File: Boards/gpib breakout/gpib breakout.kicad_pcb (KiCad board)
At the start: 2 copper layers, 51.7 x 66 mm, 18 parts, among them J1 2x12 card edge connector (let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, J2 112-024-113R001, J3 Raspberry_Pi_2_3, U1 SN75160BN, U2 SN75161BN

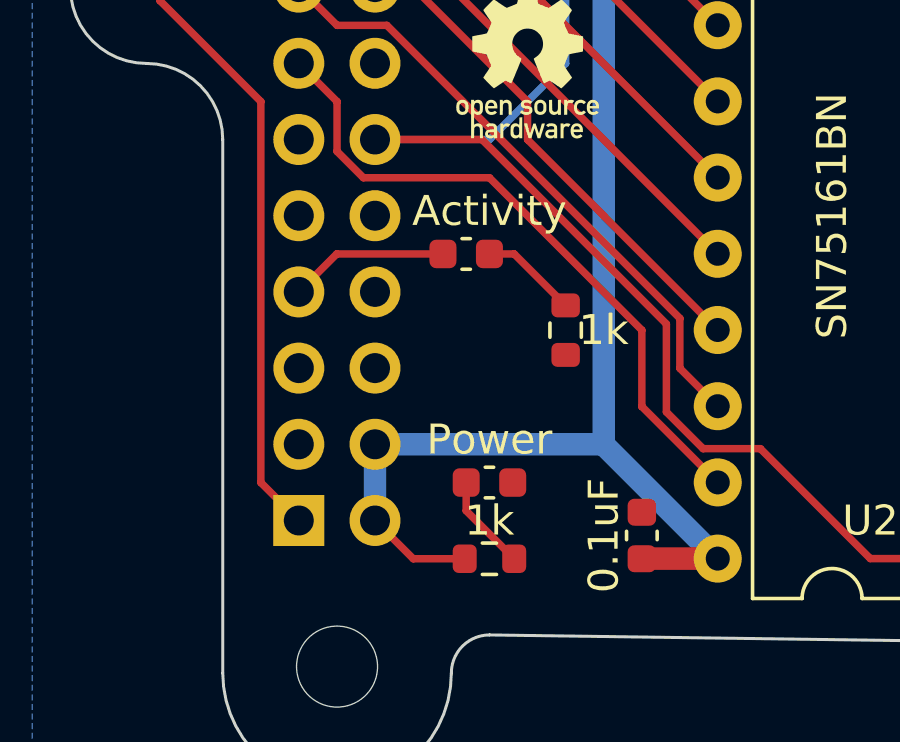
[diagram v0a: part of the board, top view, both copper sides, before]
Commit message: moved LEDs to the other side of the board
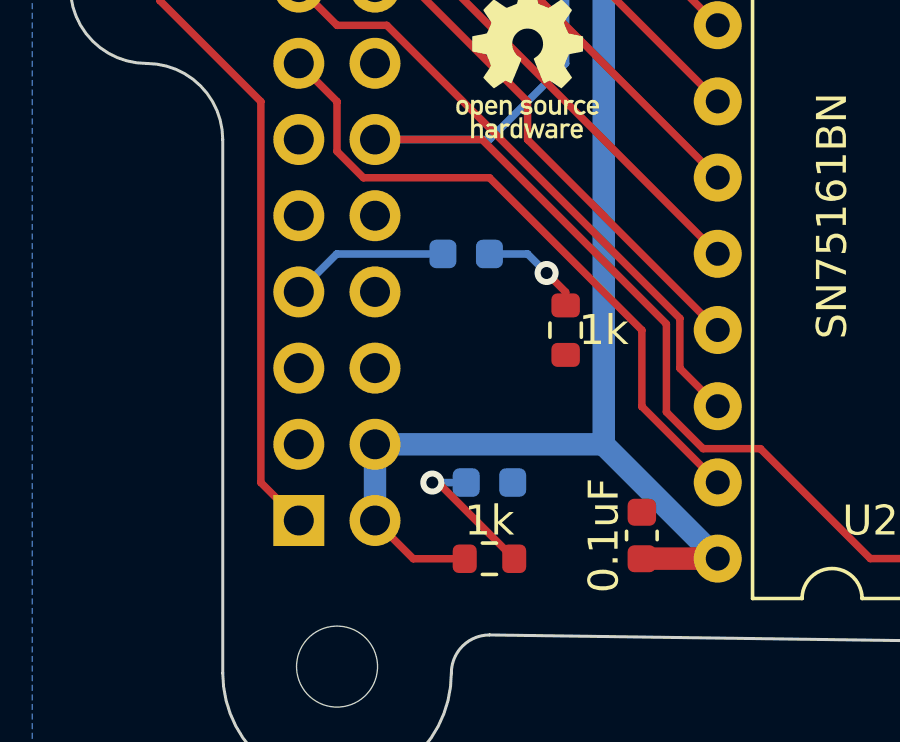
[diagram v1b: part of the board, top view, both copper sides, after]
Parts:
- D1, D2: moved to B.Cu
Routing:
- net Net-(D2-Pad2): track 3.20 -> 4.91 mm, vias 0 -> 1
- net Net-(D1-Pad1): track 3.25 -> 3.51 mm, vias 0 -> 1

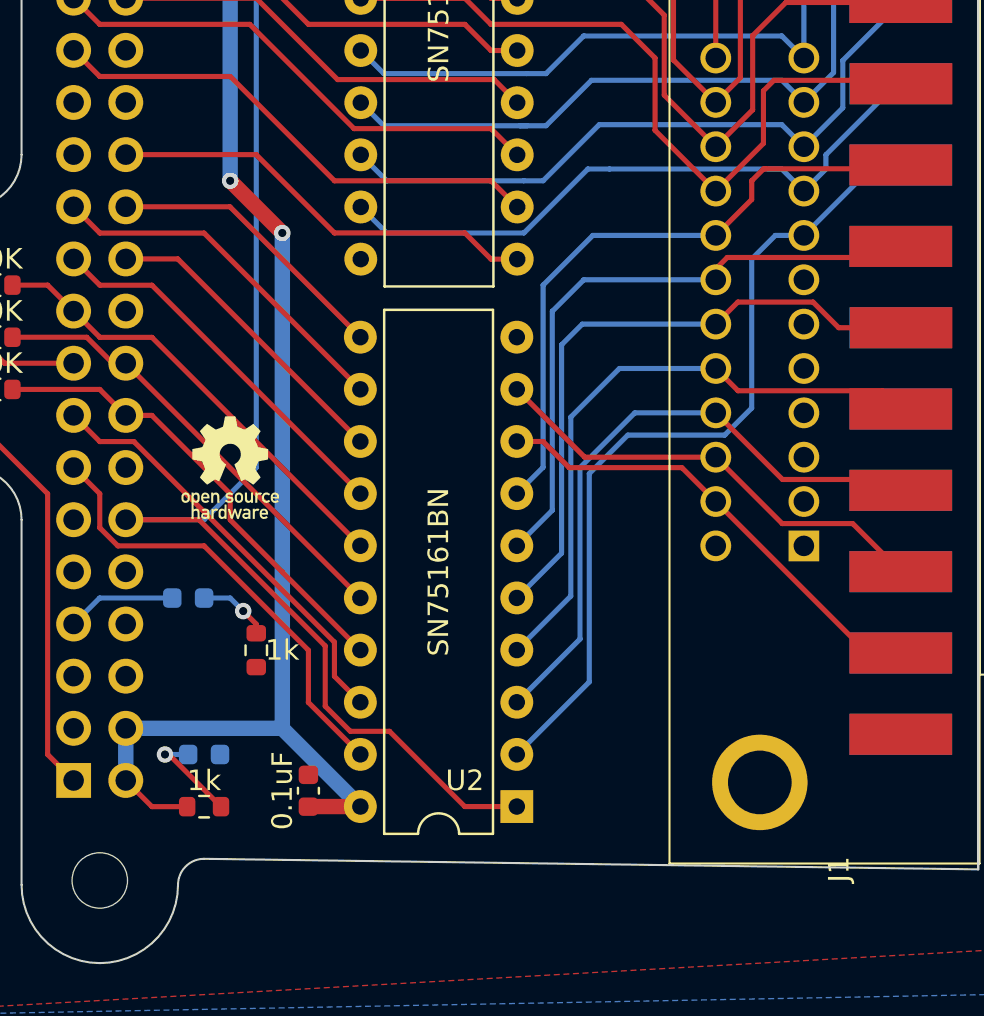
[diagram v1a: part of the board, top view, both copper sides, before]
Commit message: added gitignore
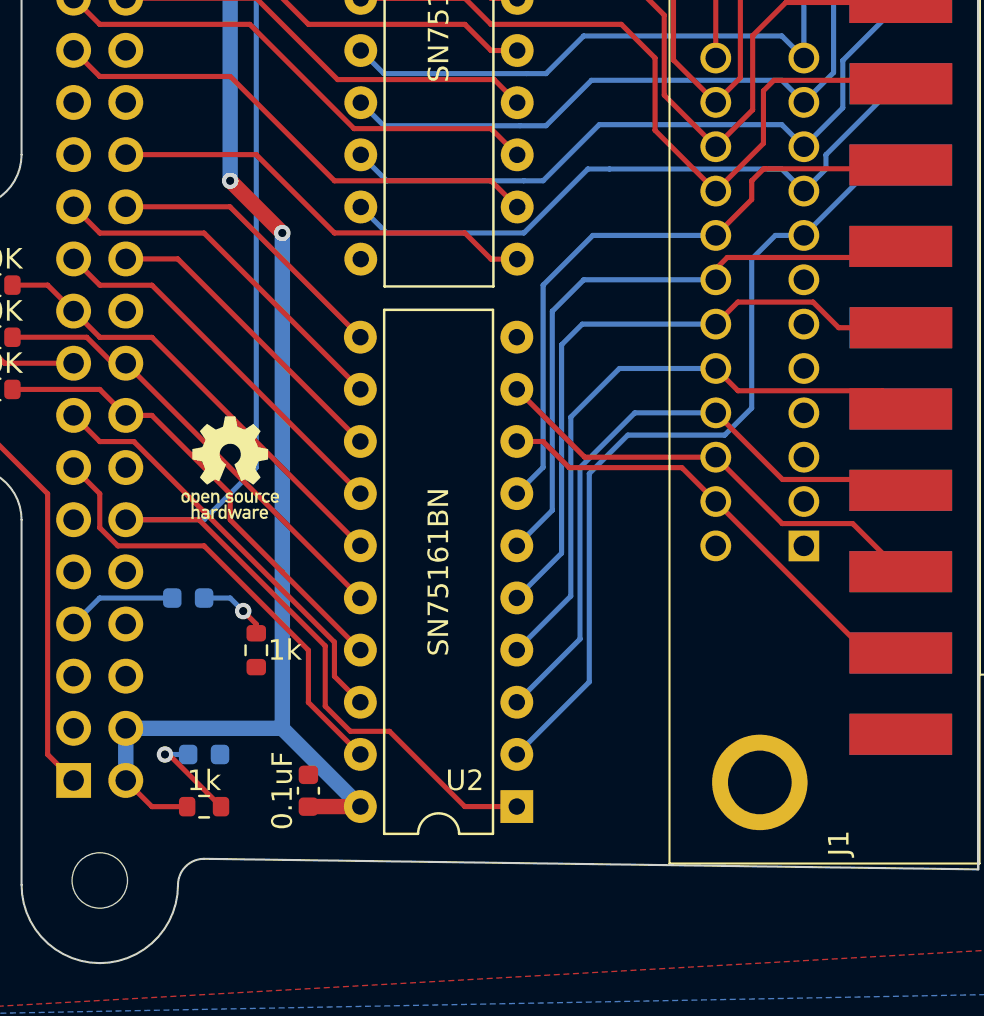
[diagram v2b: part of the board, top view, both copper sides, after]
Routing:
- net /GPIO18: track 71.2 -> 70.6 mm
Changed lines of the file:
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@@
       (layerselection 0x00010fc_ffffffff)
       (disableapertmacros false)
-      (usegerberextensions false)
+      (usegerberextensions true)
       (usegerberattributes true)
       (usegerberadvancedattributes true)
@@
       (plotinvisibletext false)
       (sketchpadsonfab false)
-      (subtractmaskfromsilk false)
+      (subtractmaskfromsilk true)
       (outputformat 1)
       (mirror false)
@@
       (effects (font (size 1 1) (thickness 0.15)))
     )
-    (fp_text value "1k" (at 0 -1.27 180) (layer "F.SilkS")
+    (fp_text value "1k" (at 0 -1.397 180) (layer "F.SilkS")
       (effects (font (size 1 1) (thickness 0.15)))
     )
@@
     (property "Sheetfile" "gpib breakout.kicad_sch")
     (property "Sheetname" "")
-    (fp_text reference "J1" (at 0 -0.5 90 unlocked) (layer "F.SilkS")
+    (fp_text reference "J1" (at 1.277 -0.5 90 unlocked) (layer "F.SilkS")
       (effects (font (size 1 1) (thickness 0.15)))
     )
@@
   (segment (start 213.224511 84.949511) (end 212.1 83.825) (width 0.25) (layer "B.Cu") (net 13))
   (segment (start 232.605489 83.115489) (end 222.954511 83.115489) (width 0.25) (layer "B.Cu") (net 13))
-  (segment (start 220.221467 87.489511) (end 219.850489 87.489511) (width 0.25) (layer "B.Cu") (net 14))
   (segment (start 235.126469 84.903531) (end 233.68 86.35) (width 0.25) (layer "B.Cu") (net 14))
   (segment (start 233.68 86.35) (end 232.605489 85.275489) (width 0.25) (layer "B.Cu") (net 14))
@@
   (segment (start 199.38 110.49) (end 198.115 111.755) (width 0.25) (layer "B.Cu") (net 20))
   (segment (start 211.591207 116.980489) (end 213.500489 116.980489) (width 0.25) (layer "F.Cu") (net 21))
-  (segment (start 201.285718 106.675) (end 200.655 106.675) (width 0.25) (layer "F.Cu") (net 21))
   (segment (start 200.655 106.675) (end 204.220292 106.675) (width 0.25) (layer "F.Cu") (net 21))
   (segment (start 210.36798 112.822688) (end 210.36798 115.757262) (width 0.25) (layer "F.Cu") (net 21))
